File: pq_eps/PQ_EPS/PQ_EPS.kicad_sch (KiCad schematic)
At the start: 80 parts, among them IC1 DS2782E+, IC2 ISL9120IRTNZ, J1 SLW-110-01-T-S, J2 SLW-110-01-T-S, J3 SLW-110-01-T-S, J4 SLW-110-01-T-S, Q1 SIR424DP-T1-GE3, U1 SPV1040TTR, U2 SPV1040TTR, U3 SPV1040TTR, U4 LTC4040EUFD#PBF

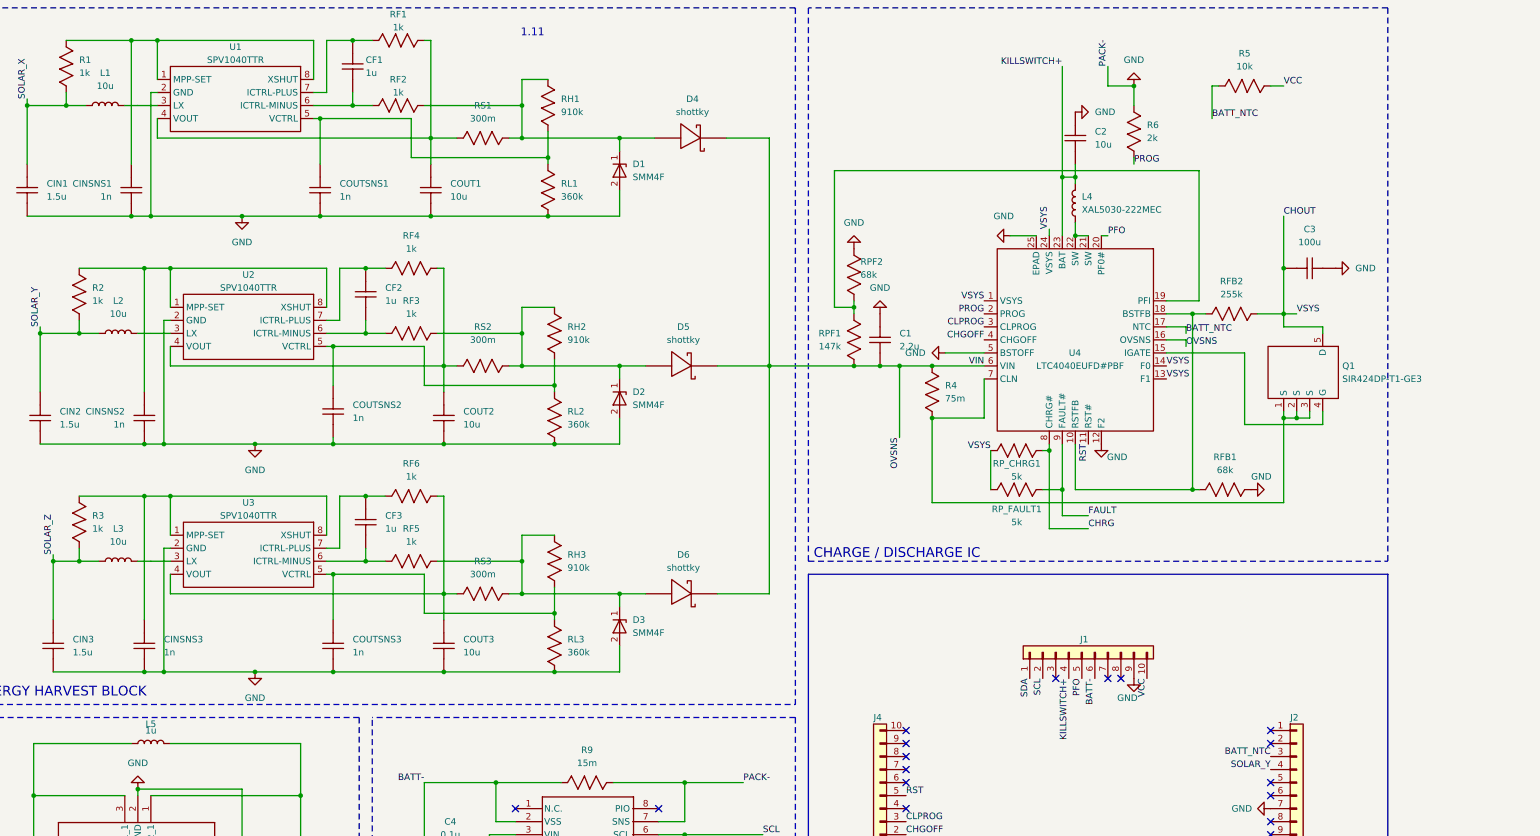
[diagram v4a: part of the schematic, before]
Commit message: Full Kicad7 transition, library improvement and adaptation, correct footprints and 3D models added
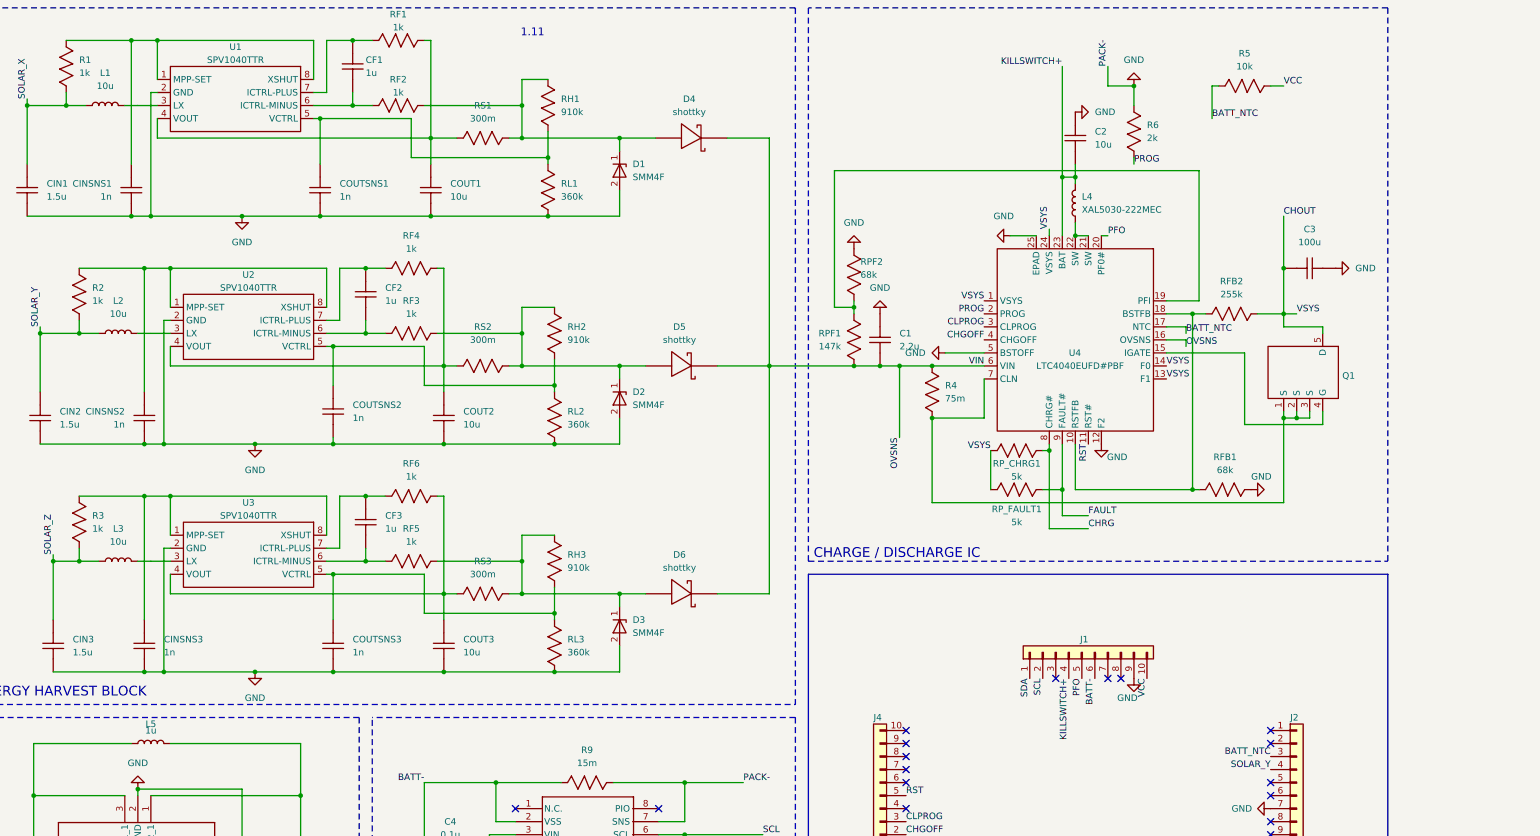
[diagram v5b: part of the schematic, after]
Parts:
- removed Q1: SIR424DP-T1-GE3, Package_SO:PowerPAK_SO-8_Single, symbol PCB-EPS-altium-import:1_SIR424DP-T1-GE3
- added Q1: ~, -nsl_power:SIR424DP, symbol -nsl_power:SIR424DP
- Annotation1: footprint symbols-nsl:Bridgemaker -> -nsl_symbols:Bridgemaker
- Annotation2: footprint symbols-nsl:NakNak -> -nsl_symbols:NakNak
- D1, D2, D3: footprint passive-nsl:SMM4F15ATR -> -nsl_passive:SMM4F15ATR
- D4, D5, D6: footprint Diode_SMD:D_SOD-128 -> -nsl_passive:RBS1LAM40ATR_Schottky; symbol PCB-EPS-altium-import:2_shottky -> -nsl_passive:RBS1LAM40ATR_Schottky
- IC2: footprint Package_DFN_QFN:QFN-12-1EP_3x3mm_P0.5mm_EP1.6x1.6mm -> -nsl_power:ISL9120IRTNZ; symbol PCB-EPS-altium-import:3_ISL9120IRTNZ -> -nsl_power:ISL9120IRTNZ
- J1, J2, J3, J4: footprint connector-nsl:SLW-110-01 -> -nsl_connector:SLW-110-01
- L4: footprint passive-nsl:XAL5030222MEC -> -nsl_passive:XAL5030222MEC
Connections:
- net CHOUT: now also Q1.5 (D)
- net at R4.1, U4.7 (CLN): now also Q1.1 (S), Q1.2 (S), Q1.3 (S)
- net at U4.15 (IGATE): now also Q1.4 (G)

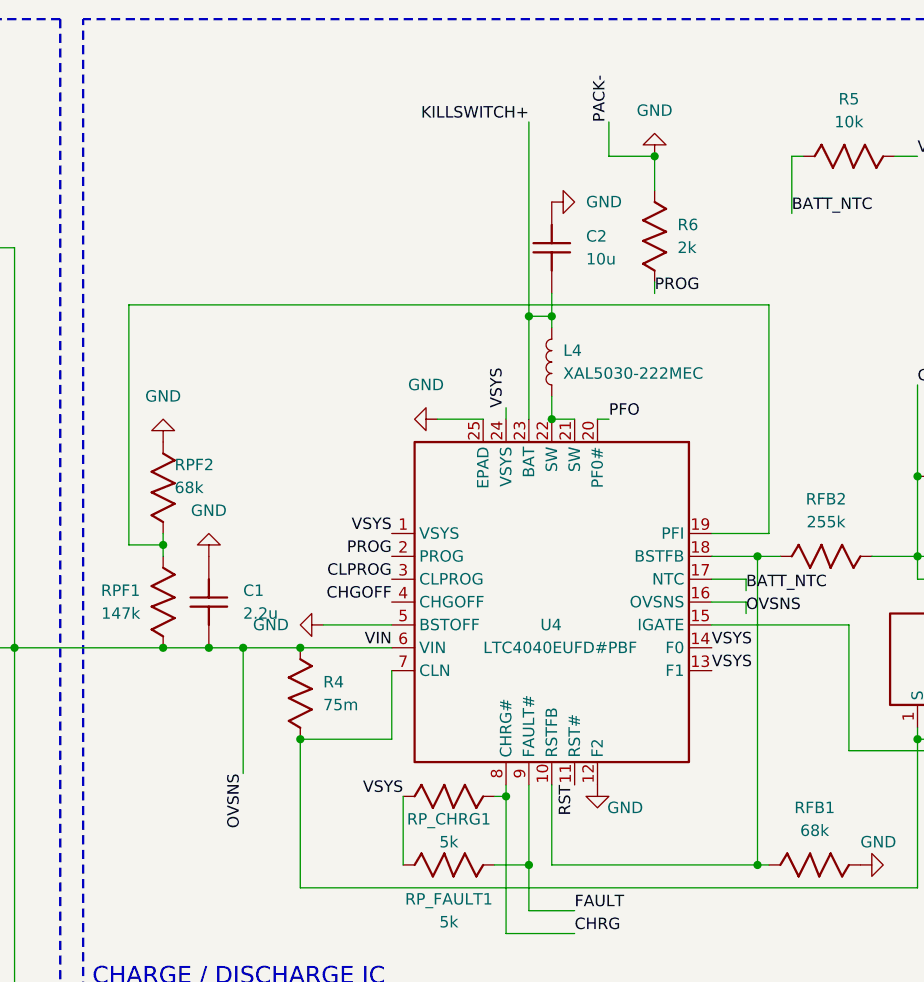
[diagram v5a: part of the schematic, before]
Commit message: Added adaptive resistive network for battery chemistry and charge voltage flexibility & connected all the PoLs + COMMS to 3V3_perm instead of VCC (3.3V - schottky diode)
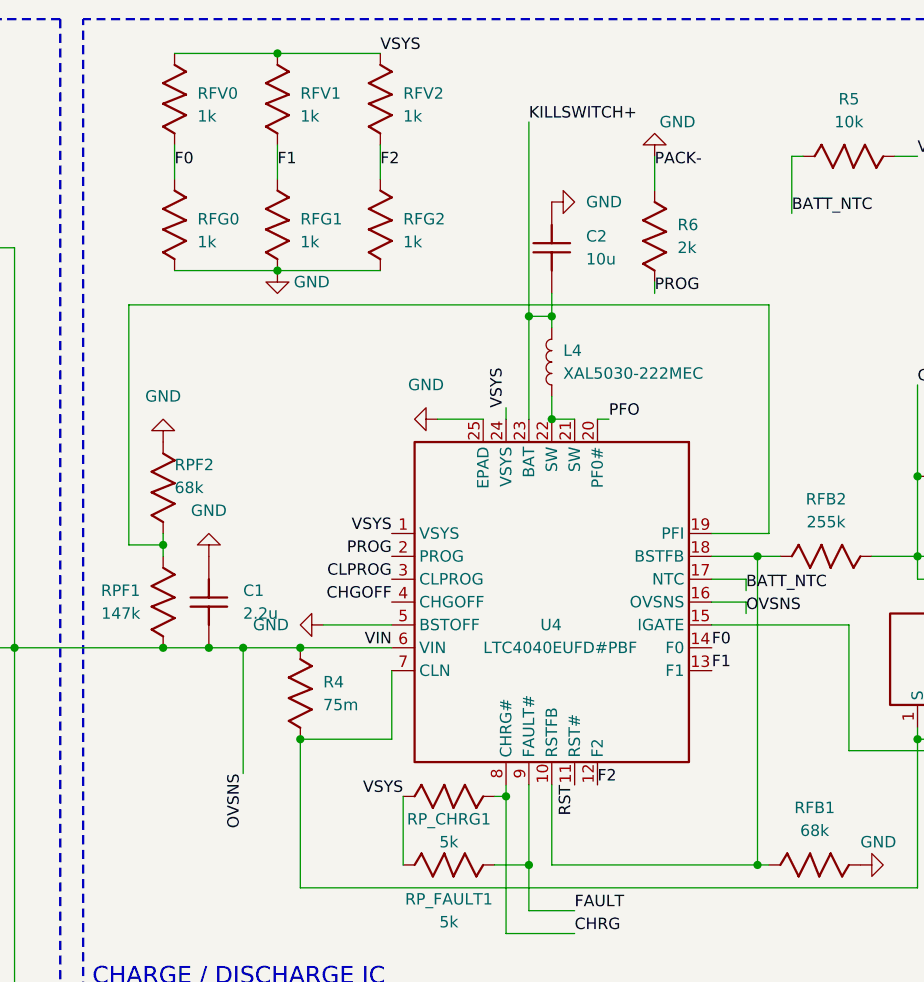
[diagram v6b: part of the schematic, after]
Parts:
- added RFG0, RFG1, RFG2, RFV0, RFV1, RFV2: 1k, Resistor_SMD:R_0603_1608Metric, symbol PCB-EPS-altium-import:1_1k
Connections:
- net CHOUT: now also RFV0.2, RFV1.2, RFV2.2; no longer U4.13 (F1), U4.14 (F0)
- net GND: now also RFG0.1, RFG1.1, RFG2.1; no longer U4.12 (F2)
- new net F0: RFG0.2, RFV0.1, U4.14 (F0)
- new net F1: RFG1.2, RFV1.1, U4.13 (F1)
- new net F2: RFG2.2, RFV2.1, U4.12 (F2)

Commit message: Small changes of component fields for the BOM
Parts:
- C1: Manufacturer 1 (none) -> Murata; Manufacturer Part Number 1 (none) -> GRM155R61C225KE11D; Supplier 1 (none) -> Mouser; Supplier Part Number 1 (none) -> 81-GRM155R61C225KE1D
- C2, COUT1, COUT2, COUT3: Manufacturer 1 (none) -> Murata; Manufacturer Part Number 1 (none) -> GRM188R61A106KAALD; Supplier 1 (none) -> Mouser; Supplier Part Number 1 (none) -> 81-GRM188R61A106KALD
- C3: Manufacturer 1 (none) -> Murata; Manufacturer Part Number 1 (none) -> GRM21BR60J107ME15K; Supplier 1 (none) -> Mouser; Supplier Part Number 1 (none) -> 81-GRM21BR60J107ME5K
- C4: Manufacturer 1 (none) -> KEMET; Manufacturer Part Number 1 (none) -> C0603C104K8PACTU; Supplier 1 (none) -> Mouser; Supplier Part Number 1 (none) -> 80-C0603C104K8P
- C5: Manufacturer 1 (none) -> Murata; Manufacturer Part Number 1 (none) -> GRM187R61A226ME15J; Supplier 1 (none) -> Mouser; Supplier Part Number 1 (none) -> 81-GRM187R61A226ME5J
- CF1, CF2, CF3: Manufacturer 1 (none) -> Murata; Manufacturer Part Number 1 (none) -> GRM155R61C105KA12D; Supplier 1 (none) -> Mouser; Supplier Part Number 1 (none) -> 81-GRM155R61C105KA2D
- CIN1, CIN2, CIN3: Manufacturer 1 (none) -> TDK; Manufacturer Part Number 1 (none) -> C1005X5R1V155K050BC; Supplier 1 (none) -> Mouser; Supplier Part Number 1 (none) -> 810-C1005X5R1V155K0C
- CINSNS1, CINSNS2, CINSNS3, COUTSNS1, COUTSNS2, COUTSNS3: Manufacturer 1 (none) -> Murata; Manufacturer Part Number 1 (none) -> GRM155R61A102KA01D; Supplier 1 (none) -> Mouser; Supplier Part Number 1 (none) -> 81-GRM155R61A102KA1D
- D4, D5, D6: Manufacturer 1 (none) -> ROHM Semiconductor; Manufacturer Part Number 1 (none) -> RBS1LAM40ATR; Supplier 1 (none) -> Mouser; Supplier Part Number 1 (none) -> 755-RBS1LAM40ATR
- DNC1, DNC2: Manufacturer 1 (none) -> Panasonic; Manufacturer Part Number 1 (none) -> ERJ-UP3J203V; Supplier 1 (none) -> Mouser; Supplier Part Number 1 (none) -> 667-ERJ-UP3J203V
- IC2: Manufacturer 1 (none) -> Renesas / Intersil; Manufacturer Part Number 1 (none) -> ISL9120IRTNZ; Supplier 1 (none) -> Farnell; Supplier Part Number 1 (none) -> 2630543
- L1, L2, L3: Manufacturer 1 (none) -> Murata; Manufacturer Part Number 1 (none) -> LQH2MPZ100MGRL; Supplier 1 (none) -> Mouser; Supplier Part Number 1 (none) -> 81-LQH2MPZ100MGRL
- L5: Manufacturer 1 (none) -> TDK; Manufacturer Part Number 1 (none) -> TFM201610GHM-1R0MTAA; Supplier 1 (none) -> Mouser; Supplier Part Number 1 (none) -> 810-TFM201610GHM1R0A
- R1, R2, R3, R8: Manufacturer 1 (none) -> -- mixed values --; Manufacturer Part Number 1 (none) -> -- mixed values --; Supplier 1 (none) -> Mouser; Supplier Part Number 1 (none) -> -- mixed values --
- R4: Manufacturer 1 (none) -> KOA Speer; Manufacturer Part Number 1 (none) -> UR73V2ATTD75L0F; Supplier 1 (none) -> Mouser; Supplier Part Number 1 (none) -> 660-UR73V2ATTD75L0F
- R5, RFB2: Manufacturer 1 (none) -> Panasonic; Manufacturer Part Number 1 (none) -> ERJ-U02F2553X; Supplier 1 (none) -> Mouser; Supplier Part Number 1 (none) -> 667-ERJ-U02F2553X
- R6: Manufacturer 1 (none) -> Panasonic; Manufacturer Part Number 1 (none) -> ERJ-UP3F1402V; Supplier 1 (none) -> Mouser; Supplier Part Number 1 (none) -> 667-ERJ-UP3F1402V
- R7: Manufacturer 1 (none) -> Panasonic; Manufacturer Part Number 1 (none) -> ERJ-UP3F5100V; Supplier 1 (none) -> Mouser; Supplier Part Number 1 (none) -> 667-ERJ-UP3F5100V
- R9: Manufacturer 1 (none) -> Vishay / Dale; Manufacturer Part Number 1 (none) -> WSLP0603R0150FEA; Supplier 1 (none) -> Mouser; Supplier Part Number 1 (none) -> 71-WSLP0603R0150FEA
- RF1, RF2, RF3, RF4, RF5, RF6: Manufacturer 1 (none) -> Vishay / Dale; Manufacturer Part Number 1 (none) -> CRCW04021K00FKEDHP; Supplier 1 (none) -> Mouser; Supplier Part Number 1 (none) -> 71-CRCW04021K00FKEDH
- RFB1, RPF2: Manufacturer 1 (none) -> KOA Speer; Manufacturer Part Number 1 (none) -> SG73P1ETTP6802F; Supplier 1 (none) -> Mouser; Supplier Part Number 1 (none) -> 660-SG73P1ETTP6802F
- RFG0, RFG1, RFG2, RFV0, RFV1, RFV2: Manufacturer 1 (none) -> Vishay / Thin Film; Manufacturer Part Number 1 (none) -> PCAN0805E1001BST5; Supplier 1 (none) -> Mouser; Supplier Part Number 1 (none) -> 71-PCAN0805E1001BST5
- RH1, RH2, RH3: Manufacturer 1 (none) -> Panasonic; Manufacturer Part Number 1 (none) -> ERJ-PA3F9103V; Supplier 1 (none) -> Mouser; Supplier Part Number 1 (none) -> 667-ERJ-PA3F9103V
- RL1, RL2, RL3: Manufacturer 1 (none) -> Panasonic; Manufacturer Part Number 1 (none) -> ERJ-UP3F3603V; Supplier 1 (none) -> Mouser; Supplier Part Number 1 (none) -> 667-ERJ-UP3F3603V
- RPF1: Manufacturer 1 (none) -> Panasonic; Manufacturer Part Number 1 (none) -> ERJ-P03F1473V; Supplier 1 (none) -> Mouser; Supplier Part Number 1 (none) -> 667-ERJ-P03F1473V
- RP_CHRG1, RP_FAULT1: Manufacturer 1 (none) -> Vishay / Dale; Manufacturer Part Number 1 (none) -> CRCW08055K00JNTA; Supplier 1 (none) -> Mouser; Supplier Part Number 1 (none) -> 71-CRCW0805J-5K
- RS1, RS2, RS3: Manufacturer 1 (none) -> ROHM Semiconductor; Manufacturer Part Number 1 (none) -> UCR03EVPFLR300; Supplier 1 (none) -> Mouser; Supplier Part Number 1 (none) -> 755-UCR03EVPFLR510
- U1, U2, U3: Manufacturer 1 (none) -> STMicroelectronics; Manufacturer Part Number 1 (none) -> SPV1040TTR; Supplier 1 (none) -> Farnell; Supplier Part Number 1 (none) -> 3129637RL
- U4: Manufacturer 1 (none) -> Analog Devices; Manufacturer Part Number 1 (none) -> LTC4040IUFD#PBF; Supplier 1 (none) -> Mouser; Supplier Part Number 1 (none) -> 584-LTC4040IUFD#PBF

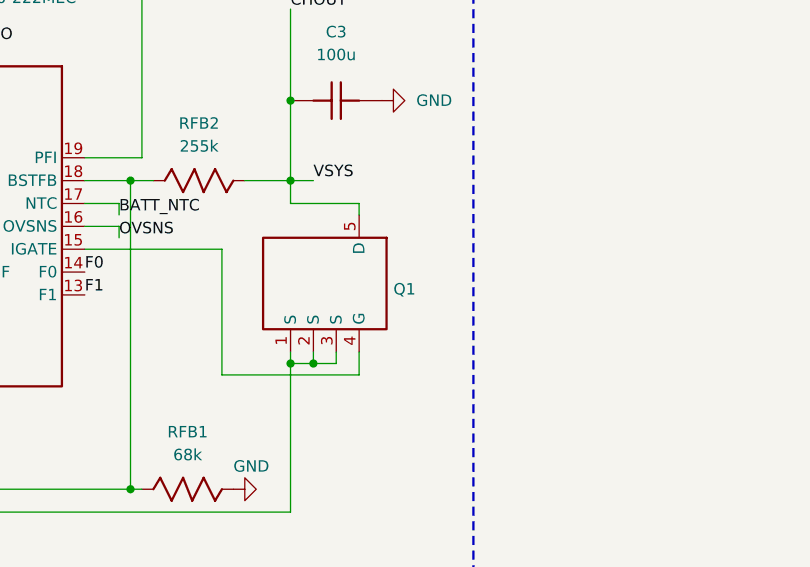
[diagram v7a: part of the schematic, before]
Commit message: BOM creation schematic changes 2.0
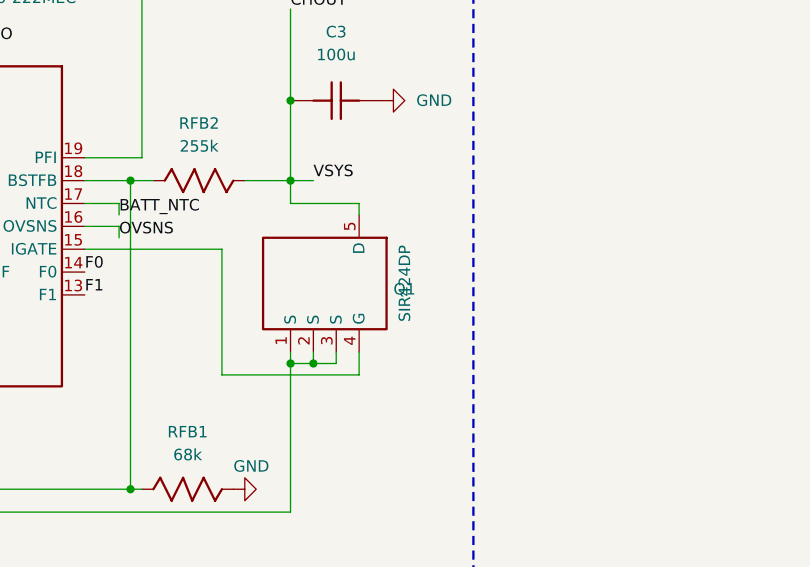
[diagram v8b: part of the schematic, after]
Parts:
- D1, D2, D3: footprint -nsl_passive:SMM4F15ATR -> DO-222AA-2; Manufacturer 1 (none) -> STMicroelectronics; Manufacturer Part Number 1 (none) -> SMM4F18A-TR; Supplier 1 (none) -> Mouser; Supplier Part Number 1 (none) -> 511-SMM4F18A-TR
- D4, D5, D6: footprint -nsl_passive:RBS1LAM40ATR_Schottky -> SOD-128-2
- H1, H2, H3, H4: Manufacturer 1 (none) -> N/A; Manufacturer Part Number 1 (none) -> N/A; Supplier 1 (none) -> N/A; Supplier Part Number 1 (none) -> N/A
- IC1: Manufacturer 1 (none) -> Analog Devices; Manufacturer Part Number 1 (none) -> DS2782E+; Supplier 1 (none) -> Mouser; Supplier Part Number 1 (none) -> 700-DS2782E
- IC2: footprint -nsl_power:ISL9120IRTNZ -> TQFN-12
- J1, J2, J3, J4: footprint -nsl_connector:SLW-110-01 -> SLW-110-01; Manufacturer 1 (none) -> Samtec; Manufacturer Part Number 1 (none) -> SLW-110-01-T-S; Supplier 1 (none) -> Mouser; Supplier Part Number 1 (none) -> 200-SLW11001TS
- L4: footprint -nsl_passive:XAL5030222MEC -> 2221; Manufacturer 1 (none) -> Coilcraft; Manufacturer Part Number 1 (none) -> XAL5030-222MEC; Supplier 1 (none) -> Mouser; Supplier Part Number 1 (none) -> 994-XAL5030-222MEC
- L5: Manufacturer Part Number 1 TFM201610GHM-1R0MTAA -> TFM201610GHM1R0A
- Q1: value ~ -> SIR424DP; footprint -nsl_power:SIR424DP -> PowerPAK-SO-8; Manufacturer 1 (none) -> Vishay; Manufacturer Part Number 1 (none) -> SIR424DP-T1-GE3; Supplier Part Number 1 (none) -> 781-SIR424DP-GE3
- R1, R2, R3, R8: Manufacturer 1 -- mixed values -- -> YAGEO; Manufacturer Part Number 1 -- mixed values -- -> RP0603BRE071KL; Supplier Part Number 1 -- mixed values -- -> 603-RP0603BRE071KL
